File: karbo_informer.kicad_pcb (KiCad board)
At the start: 2 copper layers, 12 parts, among them IC1 MAX7219, IC2 MAX7219, P1 USB_OTG

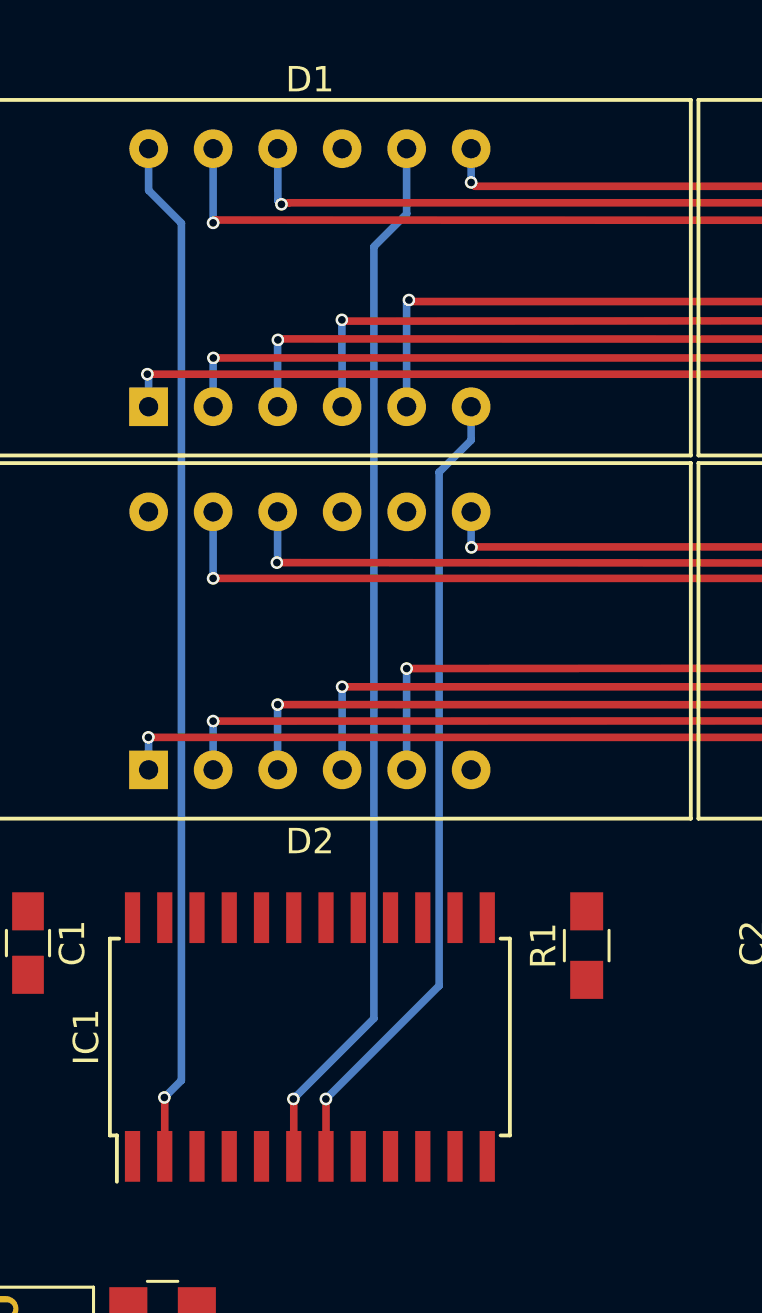
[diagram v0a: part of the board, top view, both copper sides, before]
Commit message: Wire for DIG1 to MAX7219 in the buy line
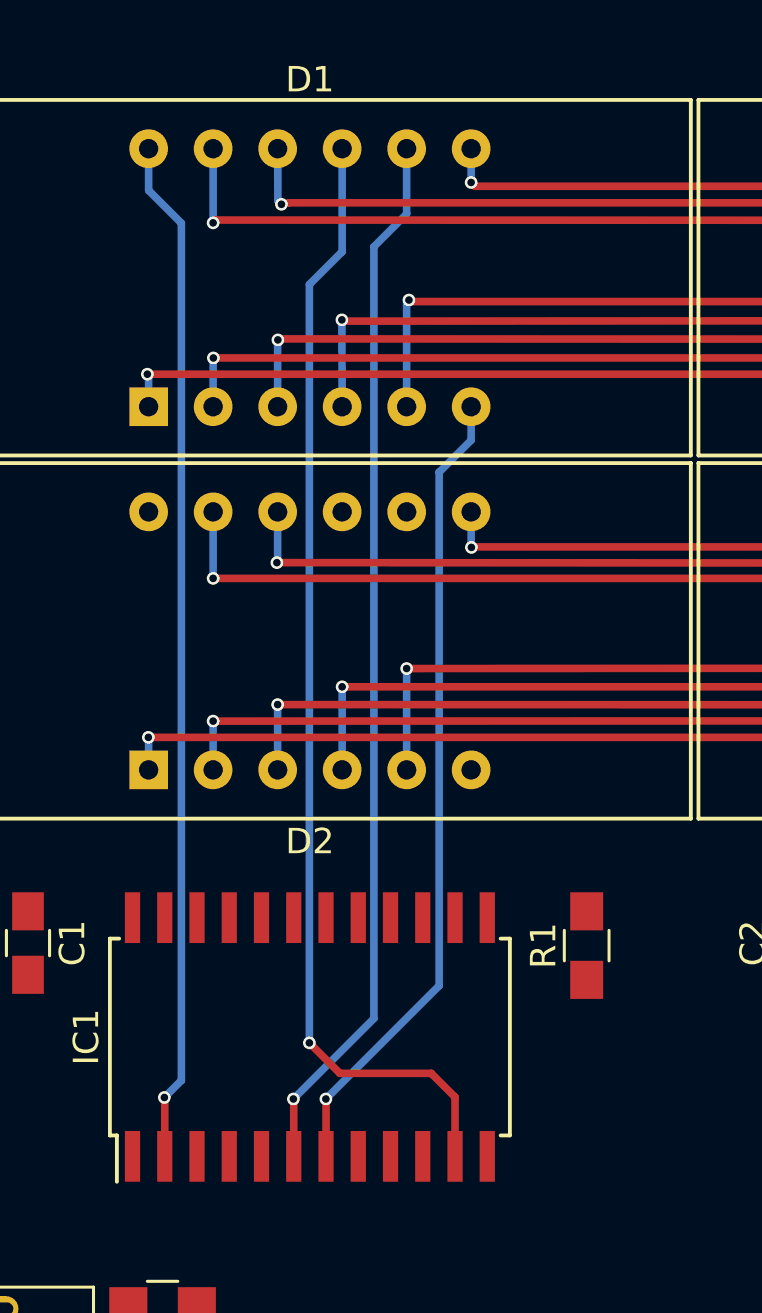
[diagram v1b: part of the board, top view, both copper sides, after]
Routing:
- net /B_DIG_1: track 0.00 -> 44.7 mm, vias 0 -> 1
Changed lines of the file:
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@@
   (general
     (links 69)
-    (no_connects 50)
+    (no_connects 49)
     (area 0 0 0 0)
     (thickness 1.6)
     (drawings 0)
-    (tracks 126)
+    (tracks 134)
     (zones 0)
     (modules 12)
@@
   (segment (start 34.45 25.46) (end 35.74 26.75) (width 0.3) (layer B.Cu) (net 9))
   (segment (start 34.45 23.82) (end 34.45 25.46) (width 0.3) (layer B.Cu) (net 9))
+  (segment (start 42.07 23.82) (end 42.07 27.88) (width 0.3) (layer B.Cu) (net 10) (status 400000))
+  (segment (start 46.515 61.165) (end 46.515 63.5) (width 0.3) (layer F.Cu) (net 10) (status 800000))
+  (segment (start 45.58 60.23) (end 46.515 61.165) (width 0.3) (layer F.Cu) (net 10))
+  (segment (start 41.98 60.23) (end 45.58 60.23) (width 0.3) (layer F.Cu) (net 10))
+  (segment (start 40.78 59.03) (end 41.98 60.23) (width 0.3) (layer F.Cu) (net 10))
+  (via (at 40.78 59.03) (size 0.5) (drill 0.3) (layers F.Cu B.Cu) (net 10))
+  (segment (start 40.78 29.17) (end 40.78 59.03) (width 0.3) (layer B.Cu) (net 10))
+  (segment (start 42.07 27.88) (end 40.78 29.17) (width 0.3) (layer B.Cu) (net 10))
   (segment (start 44.61 23.82) (end 44.61 26.39) (width 0.3) (layer B.Cu) (net 11) (status 400000))
   (segment (start 40.165 61.255) (end 40.165 63.5) (width 0.3) (layer F.Cu) (net 11) (status 800000))

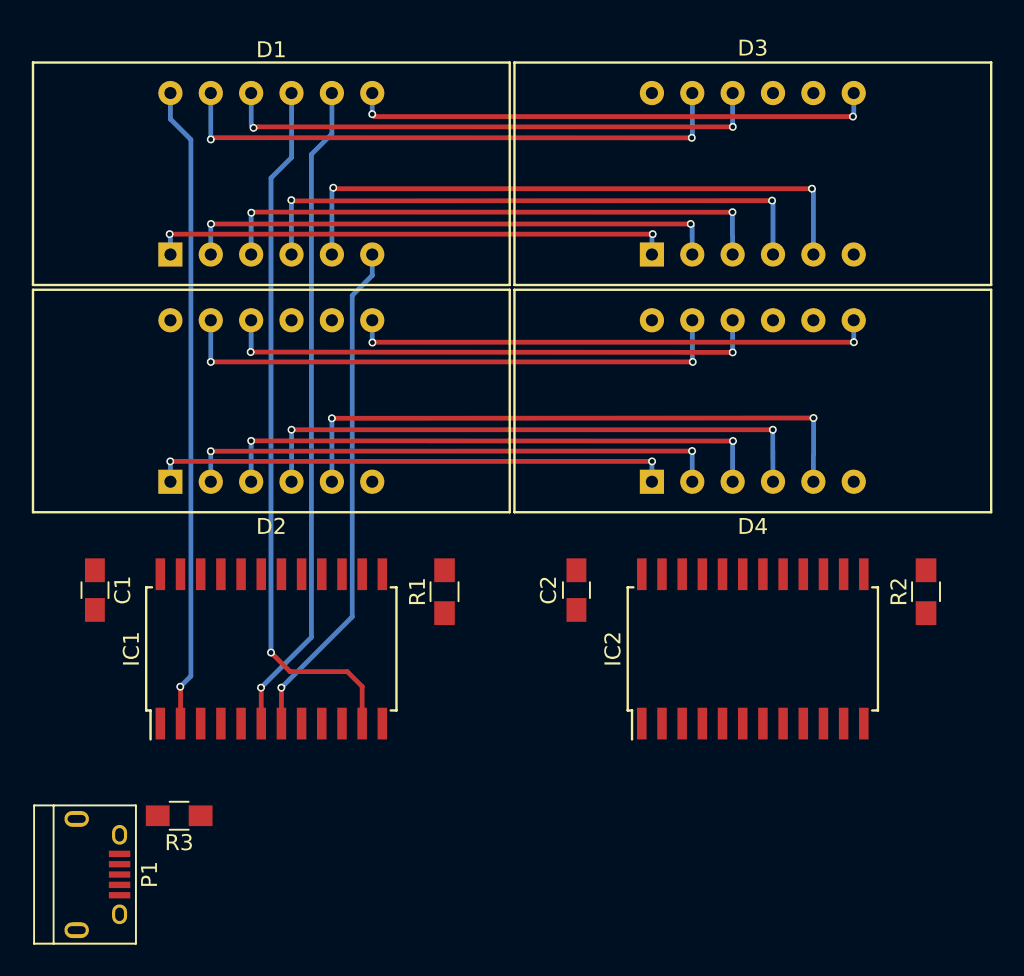
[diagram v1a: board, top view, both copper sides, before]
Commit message: Same update to buy line wires
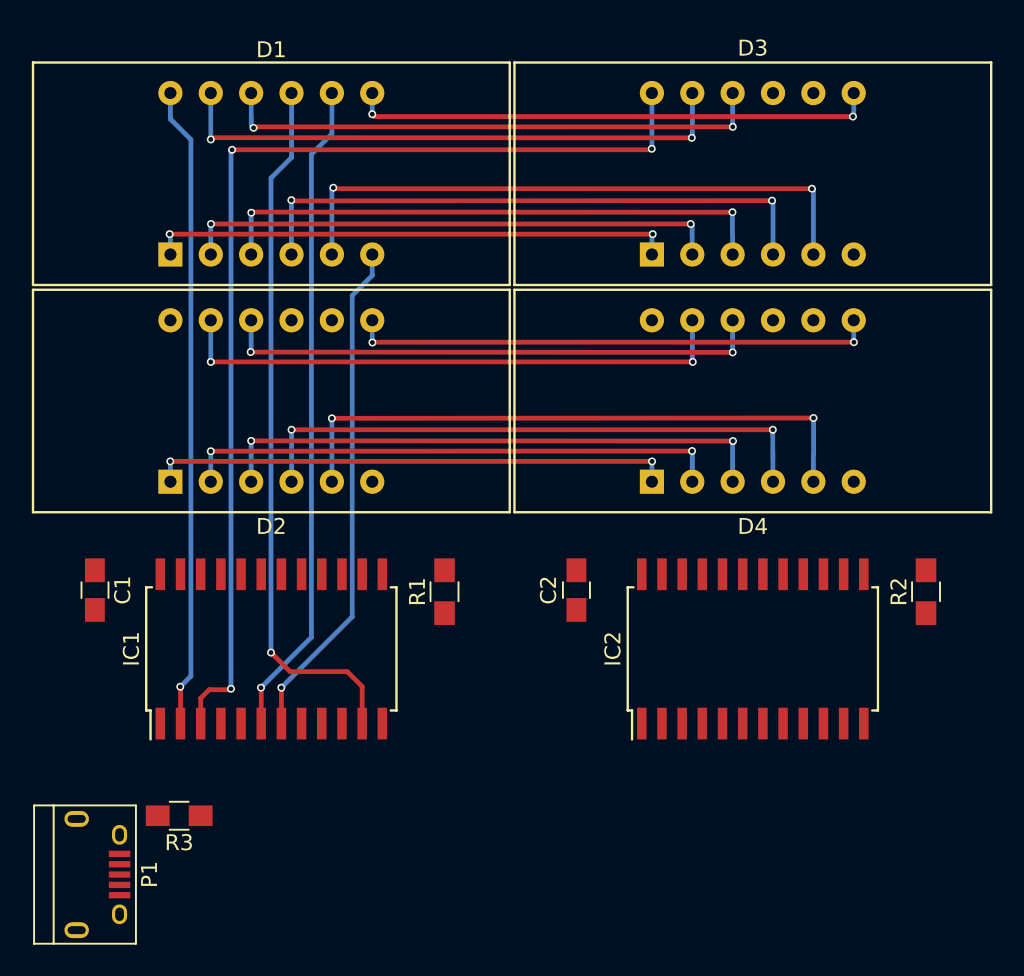
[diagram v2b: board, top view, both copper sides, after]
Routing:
- net /B_DIG_4: track 0.00 -> 67.6 mm, vias 0 -> 3
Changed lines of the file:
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@@
   (general
     (links 69)
-    (no_connects 49)
+    (no_connects 48)
     (area 0 0 0 0)
     (thickness 1.6)
     (drawings 0)
-    (tracks 134)
+    (tracks 147)
     (zones 0)
     (modules 12)
@@
   (via (at 44.7 29.78) (size 0.5) (drill 0.3) (layers F.Cu B.Cu) (net 5))
   (segment (start 44.61 29.87) (end 44.7 29.78) (width 0.3) (layer B.Cu) (net 5))
-  (segment (start 47.15 33.98) (end 47.15 35.3) (width 0.3) (layer B.Cu) (net 6) (status 400000))
-  (segment (start 41.435 61.245) (end 41.435 63.5) (width 0.3) (layer F.Cu) (net 6) (status 800000))
+  (segment (start 47.15 33.98) (end 47.15 35.3) (width 0.3) (layer B.Cu) (net 6))
+  (segment (start 41.435 61.245) (end 41.435 63.5) (width 0.3) (layer F.Cu) (net 6))
   (segment (start 41.43 61.24) (end 41.435 61.245) (width 0.3) (layer F.Cu) (net 6))
   (via (at 41.43 61.24) (size 0.5) (drill 0.3) (layers F.Cu B.Cu) (net 6))
@@
   (segment (start 34.45 25.46) (end 35.74 26.75) (width 0.3) (layer B.Cu) (net 9))
   (segment (start 34.45 23.82) (end 34.45 25.46) (width 0.3) (layer B.Cu) (net 9))
-  (segment (start 42.07 23.82) (end 42.07 27.88) (width 0.3) (layer B.Cu) (net 10) (status 400000))
-  (segment (start 46.515 61.165) (end 46.515 63.5) (width 0.3) (layer F.Cu) (net 10) (status 800000))
+  (segment (start 42.07 23.82) (end 42.07 27.88) (width 0.3) (layer B.Cu) (net 10))
+  (segment (start 46.515 61.165) (end 46.515 63.5) (width 0.3) (layer F.Cu) (net 10))
   (segment (start 45.58 60.23) (end 46.515 61.165) (width 0.3) (layer F.Cu) (net 10))
   (segment (start 41.98 60.23) (end 45.58 60.23) (width 0.3) (layer F.Cu) (net 10))
@@
   (segment (start 40.78 29.17) (end 40.78 59.03) (width 0.3) (layer B.Cu) (net 10))
   (segment (start 42.07 27.88) (end 40.78 29.17) (width 0.3) (layer B.Cu) (net 10))
-  (segment (start 44.61 23.82) (end 44.61 26.39) (width 0.3) (layer B.Cu) (net 11) (status 400000))
-  (segment (start 40.165 61.255) (end 40.165 63.5) (width 0.3) (layer F.Cu) (net 11) (status 800000))
+  (segment (start 44.61 23.82) (end 44.61 26.39) (width 0.3) (layer B.Cu) (net 11))
+  (segment (start 40.165 61.255) (end 40.165 63.5) (width 0.3) (layer F.Cu) (net 11))
   (segment (start 40.15 61.24) (end 40.165 61.255) (width 0.3) (layer F.Cu) (net 11))
   (via (at 40.15 61.24) (size 0.5) (drill 0.3) (layers F.Cu B.Cu) (net 11))
@@
   (segment (start 47.18 39.5) (end 77.46 39.5) (width 0.3) (layer F.Cu) (net 24))
   (via (at 47.16 39.52) (size 0.5) (drill 0.3) (layers F.Cu B.Cu) (net 24))
+  (segment (start 36.355 61.905) (end 36.355 63.5) (width 0.3) (layer F.Cu) (net 26))
+  (segment (start 36.89 61.37) (end 36.355 61.905) (width 0.3) (layer F.Cu) (net 26))
+  (segment (start 38.2 61.37) (end 36.89 61.37) (width 0.3) (layer F.Cu) (net 26))
+  (segment (start 38.26 61.31) (end 38.2 61.37) (width 0.3) (layer F.Cu) (net 26))
+  (via (at 38.26 61.31) (size 0.5) (drill 0.3) (layers F.Cu B.Cu) (net 26))
+  (segment (start 38.26 27.46) (end 38.26 61.31) (width 0.3) (layer B.Cu) (net 26))
+  (segment (start 38.33 27.39) (end 38.26 27.46) (width 0.3) (layer B.Cu) (net 26))
+  (via (at 38.33 27.39) (size 0.5) (drill 0.3) (layers F.Cu B.Cu) (net 26))
+  (segment (start 64.68 27.39) (end 38.33 27.39) (width 0.3) (layer F.Cu) (net 26))
+  (segment (start 64.74 27.33) (end 64.68 27.39) (width 0.3) (layer F.Cu) (net 26))
+  (via (at 64.74 27.33) (size 0.5) (drill 0.3) (layers F.Cu B.Cu) (net 26))
+  (segment (start 64.75 27.32) (end 64.74 27.33) (width 0.3) (layer B.Cu) (net 26))
+  (segment (start 64.75 23.82) (end 64.75 27.32) (width 0.3) (layer B.Cu) (net 26))
 )

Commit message: Wire for DIG4 to MAX7219 in the buy line
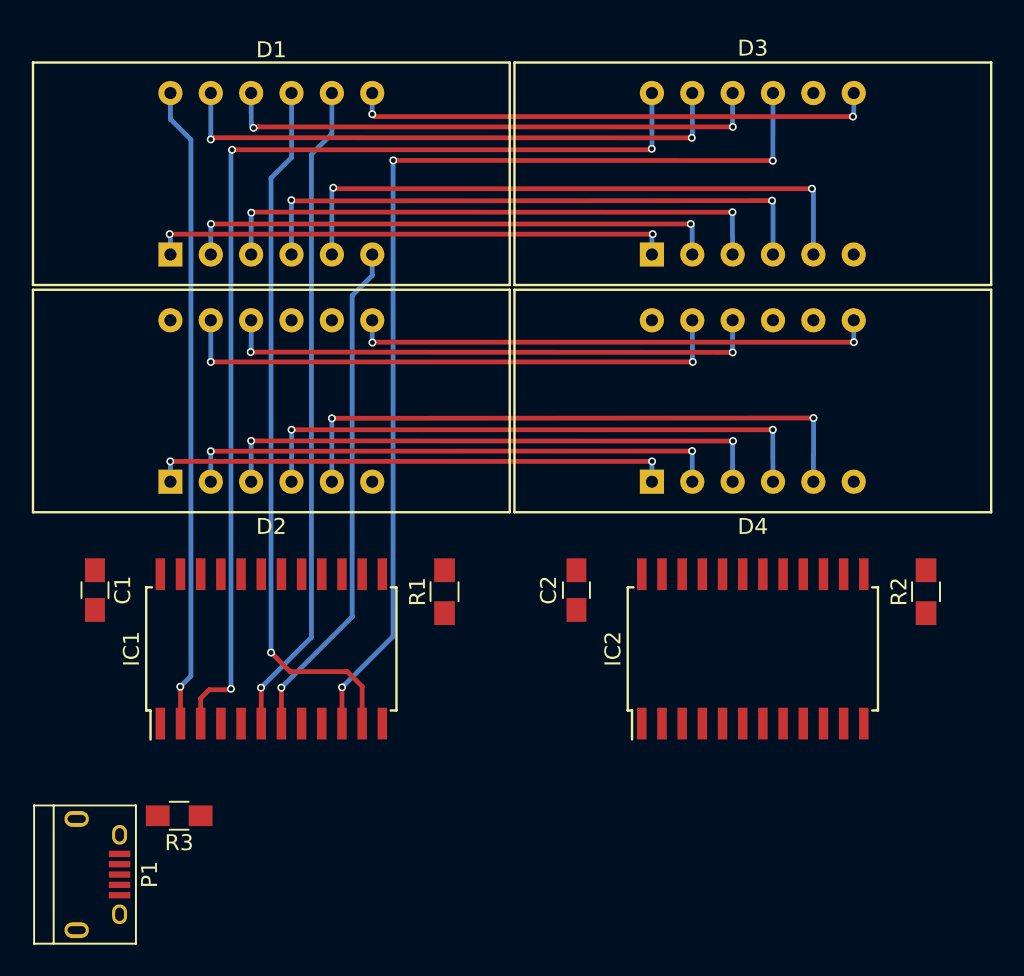
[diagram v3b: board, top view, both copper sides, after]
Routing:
- net /B_DIG_5: track 0.00 -> 64.9 mm, vias 0 -> 3
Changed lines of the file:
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@@
   (general
     (links 69)
-    (no_connects 48)
+    (no_connects 47)
     (area 0 0 0 0)
     (thickness 1.6)
     (drawings 0)
-    (tracks 147)
+    (tracks 157)
     (zones 0)
     (modules 12)
@@
   (segment (start 64.75 27.32) (end 64.74 27.33) (width 0.3) (layer B.Cu) (net 26))
   (segment (start 64.75 23.82) (end 64.75 27.32) (width 0.3) (layer B.Cu) (net 26))
+  (via (at 48.47 28.06) (size 0.5) (drill 0.3) (layers F.Cu B.Cu) (net 27))
+  (segment (start 72.34 28.07) (end 48.47 28.06) (width 0.3) (layer F.Cu) (net 27))
+  (via (at 72.36 28.08) (size 0.5) (drill 0.3) (layers F.Cu B.Cu) (net 27))
+  (segment (start 45.245 61.225) (end 45.245 63.5) (width 0.3) (layer F.Cu) (net 27) (status 800000))
+  (segment (start 45.25 61.22) (end 45.245 61.225) (width 0.3) (layer F.Cu) (net 27))
+  (via (at 45.25 61.22) (size 0.5) (drill 0.3) (layers F.Cu B.Cu) (net 27))
+  (segment (start 48.46 58.01) (end 45.25 61.22) (width 0.3) (layer B.Cu) (net 27))
+  (segment (start 48.46 28.07) (end 48.46 58.01) (width 0.3) (layer B.Cu) (net 27))
+  (segment (start 48.47 28.06) (end 48.46 28.07) (width 0.3) (layer B.Cu) (net 27))
+  (segment (start 72.37 23.82) (end 72.36 28.08) (width 0.3) (layer B.Cu) (net 27) (status 400000))
 )
